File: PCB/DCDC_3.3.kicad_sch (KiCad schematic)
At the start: 21 parts, among them U1 HT75xx-1-SOT89, U10 LV2842XLVDDCR

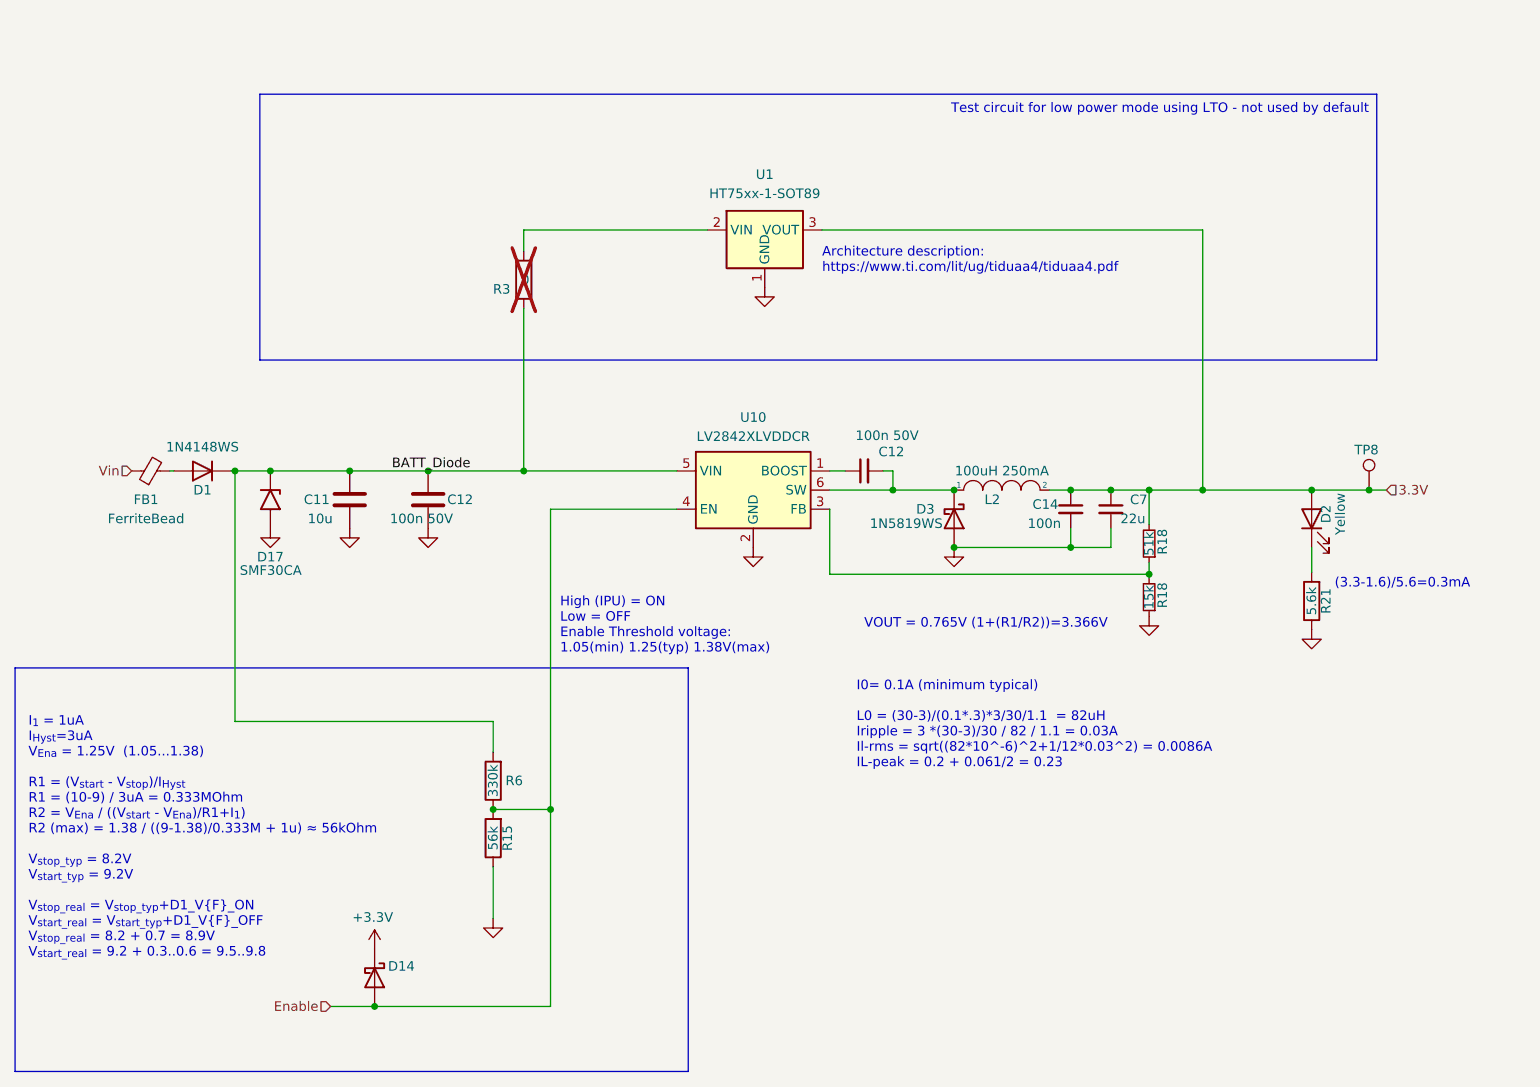
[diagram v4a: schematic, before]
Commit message: Added jumper for the DCDC enable line
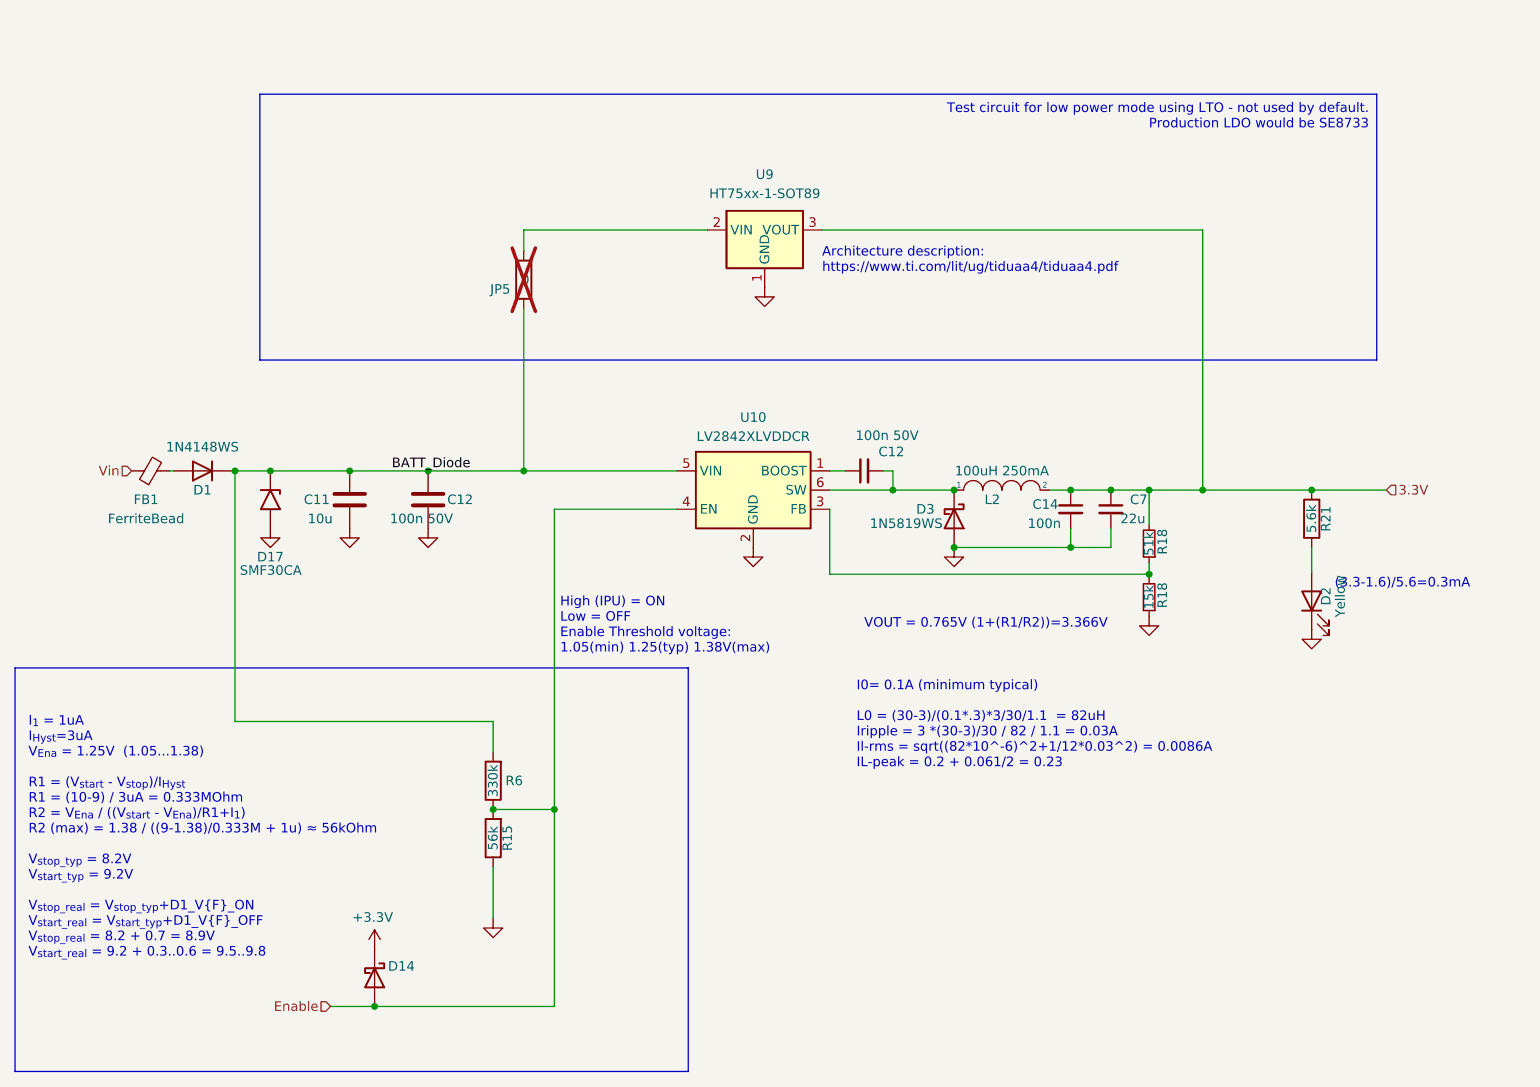
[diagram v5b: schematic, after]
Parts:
- removed TP8: WirePad, TestPoint:TestPoint_Pad_D1.0mm, symbol Connector:TestPoint
- renumbered R3 to JP5, U1 to U9
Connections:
- net 3.3V: now also R21.2; no longer D2.2 (A)
- net GND: now also D2.1 (K); no longer R21.1
- new net: D2.2 (A), R21.1
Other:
- moved on the sheet: D2, R21

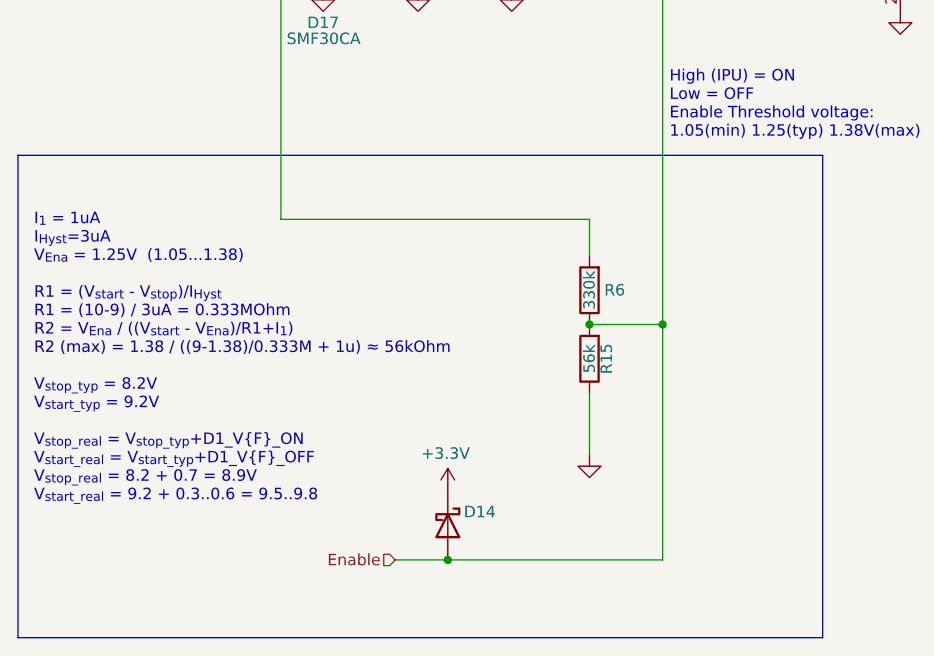
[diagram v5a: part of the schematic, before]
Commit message: Added undervoltage shutdown filter
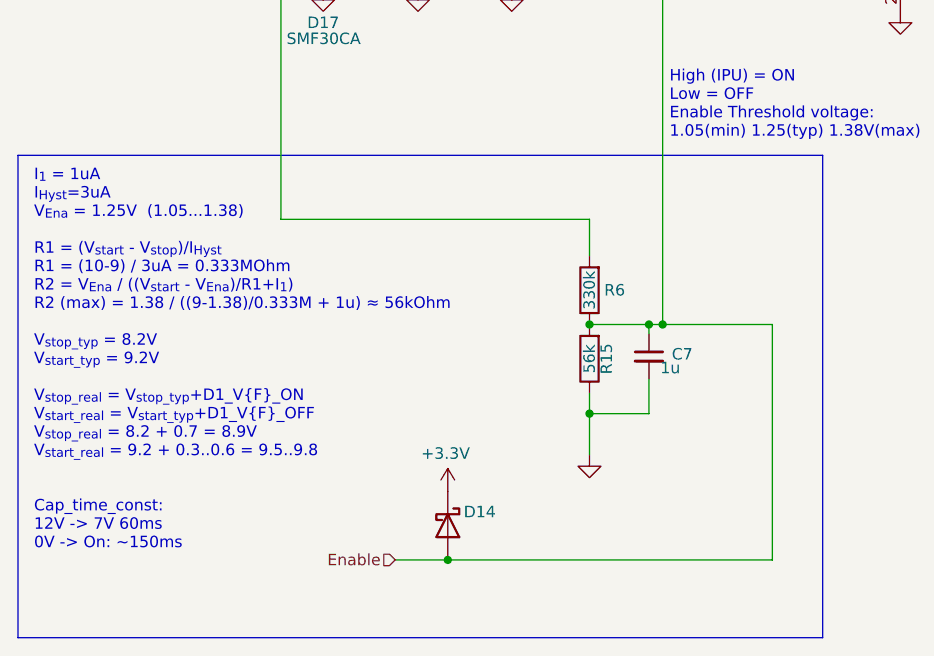
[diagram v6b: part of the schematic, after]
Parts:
- added C7: 1u, Capacitor_SMD:C_0402_1005Metric, symbol Device:C_Small
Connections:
- net Enable: now also C7.1
- net GND: now also C7.2
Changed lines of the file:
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@@
 (kicad_sch (version 20230121) (generator eeschema)
   (paper "A4")
+  (junction (at 101.6 134.874) (diameter 0) (color 0 0 0 0)
+  )
   (junction (at 105.664 80.01) (diameter 0) (color 0 0 0 0)
   )
@@
   (junction (at 178.308 82.55) (diameter 0) (color 0 0 0 0)
   )
+  (junction (at 108.204 124.968) (diameter 0) (color 0 0 0 0)
+  )
   (junction (at 82.55 80.01) (diameter 0) (color 0 0 0 0)
   )
@@
     (stroke (width 0) (type default))
   )
+  (wire (pts (xy 121.92 124.968) (xy 109.728 124.968))
+    (stroke (width 0) (type default))
+  )
   (wire (pts (xy 195.834 82.55) (xy 210.312 82.55))
     (stroke (width 0) (type default))
@@
     (stroke (width 0) (type default))
   )
+  (wire (pts (xy 108.204 124.968) (xy 109.728 124.968))
+    (stroke (width 0) (type default))
+  )
   (wire (pts (xy 188.722 92.202) (xy 188.722 93.726))
     (stroke (width 0) (type default))
@@
     (stroke (width 0) (type default))
   )
+  (wire (pts (xy 108.204 131.064) (xy 108.204 134.874))
+    (stroke (width 0) (type default))
+  )
   (wire (pts (xy 67.31 113.284) (xy 101.6 113.284))
     (stroke (width 0) (type default))
   )
-  (wire (pts (xy 101.6 132.588) (xy 101.6 139.446))
+  (wire (pts (xy 101.6 132.588) (xy 101.6 134.874))
     (stroke (width 0) (type default))
   )
@@
     (stroke (width 0) (type default))
   )
-  (wire (pts (xy 109.728 124.968) (xy 109.728 151.13))
+  (wire (pts (xy 121.92 124.968) (xy 121.92 151.13))
     (stroke (width 0) (type default))
   )
@@
     (stroke (width 0) (type default))
   )
+  (wire (pts (xy 108.204 134.874) (xy 101.6 134.874))
+    (stroke (width 0) (type default))
+  )
   (wire (pts (xy 59.182 80.01) (xy 58.674 80.01))
     (stroke (width 0) (type default))
@@
     (stroke (width 0) (type default))
   )
+  (wire (pts (xy 108.204 125.984) (xy 108.204 124.968))
+    (stroke (width 0) (type default))
+  )
   (wire (pts (xy 162.814 90.17) (xy 178.308 90.17))
     (stroke (width 0) (type default))
@@
     (stroke (width 0) (type default))
   )
-  (wire (pts (xy 85.852 151.13) (xy 109.728 151.13))
+  (wire (pts (xy 85.852 151.13) (xy 121.92 151.13))
+    (stroke (width 0) (type default))
+  )
+  (wire (pts (xy 101.6 124.968) (xy 108.204 124.968))
     (stroke (width 0) (type default))
   )
@@
     (stroke (width 0) (type default))
   )
-  (wire (pts (xy 101.6 124.968) (xy 109.728 124.968))
+  (wire (pts (xy 101.6 134.874) (xy 101.6 139.446))
     (stroke (width 0) (type default))
   )
@@
     (effects (font (size 1.27 1.27)) (justify left bottom))
   )
-  (text "I_{1} = 1uA\nI_{Hyst}=3uA\nV_{Ena} = 1.25V  (1.05...1.38)\n\nR1 = (V_{start} - V_{stop})/I_{Hyst}\nR1 = (10-9) / 3uA = 0.333MOhm\nR2 = V_{Ena} / ((V_{start} - V_{Ena})/R1+I_{1})\nR2 (max) = 1.38 / ((9-1.38)/0.333M + 1u) ≈ 56kOhm\n\nV_{stop_typ} = 8.2V\nV_{start_typ} = 9.2V\n\nV_{stop_real} = V_{stop_typ}+D1_V{F}_ON\nV_{start_real} = V_{start_typ}+D1_V{F}_OFF\nV_{stop_real} = 8.2 + 0.7 = 8.9V\nV_{start_real} = 9.2 + 0.3..0.6 = 9.5..9.8"
-    (at 39.878 144.78 0)
-    (effects (font (size 1.27 1.27)) (justify left bottom))
+  (text "I_{1} = 1uA\nI_{Hyst}=3uA\nV_{Ena} = 1.25V  (1.05...1.38)\n\nR1 = (V_{start} - V_{stop})/I_{Hyst}\nR1 = (10-9) / 3uA = 0.333MOhm\nR2 = V_{Ena} / ((V_{start} - V_{Ena})/R1+I_{1})\nR2 (max) = 1.38 / ((9-1.38)/0.333M + 1u) ≈ 56kOhm\n\nV_{stop_typ} = 8.2V\nV_{start_typ} = 9.2V\n\nV_{stop_real} = V_{stop_typ}+D1_V{F}_ON\nV_{start_real} = V_{start_typ}+D1_V{F}_OFF\nV_{stop_real} = 8.2 + 0.7 = 8.9V\nV_{start_real} = 9.2 + 0.3..0.6 = 9.5..9.8\n\n\nCap_time_const:\n12V -> 7V 60ms\n0V -> On: ~150ms"
+    (at 39.878 150.114 0)
+    (effects (font (size 1.27 1.27)) (justify left bottom) (href "https://everycircuit.com/circuit/6478510418558976"))
   )
   (text "I0= 0.1A (minimum typical)\n\nL0 = (30-3)/(0.1*.3)*3/30/1.1  = 82uH\nIripple = 3 *(30-3)/30 / 82 / 1.1 = 0.03A\nIl-rms = sqrt((82*10^-6)^2+1/12*0.03^2) = 0.0086A\nIL-peak = 0.2 + 0.061/2 = 0.23\n\n"
@@
         )
       )
+    )
+  )
+  (symbol (lib_id "Device:C_Small") (at 108.204 128.524 0) (unit 1)
+    (in_bom yes) (on_board yes) (dnp no)
+    (property "Reference" "C7" (at 110.744 128.27 0)
+      (effects (font (size 1.27 1.27)) (justify left))
+    )
+    (property "Value" "1u" (at 109.474 129.794 0)
+      (effects (font (size 1.27 1.27)) (justify left))
+    )
+    (property "Footprint" "Capacitor_SMD:C_0402_1005Metric" (at 108.204 128.524 0)
+      (effects (font (size 1.27 1.27)) hide)
+    )
+    (property "Datasheet" "https://weblib.samsungsem.com/mlcc/mlcc-ec-data-sheet.do?partNumber=CL05A105KA5NQN" (at 108.204 128.524 0)
+      (effects (font (size 1.27 1.27)) hide)
+    )
+    (property "LCSC" "C52923" (at 110.744 127.2602 0)
+      (effects (font (size 1.27 1.27)) hide)
+    )
+    (pin "1")
+    (pin "2")
+    (instances
+      (project "StepperServoCAN"
+        (path "/92dad13e-412a-43d4-9260-9087579302b1"
+          (reference "C7") (unit 1)
+        )
+        (path "/92dad13e-412a-43d4-9260-9087579302b1/82f027ad-2d00-453d-ab1c-0ba3b5cb1ef7"
+          (reference "C38") (unit 1)
+        )
+      )

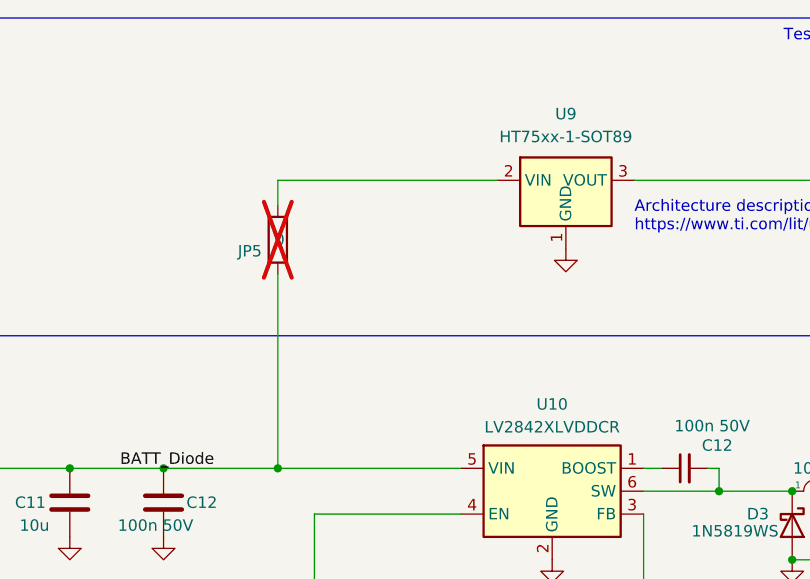
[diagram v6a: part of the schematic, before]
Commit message: Added UART/I2C aux connector
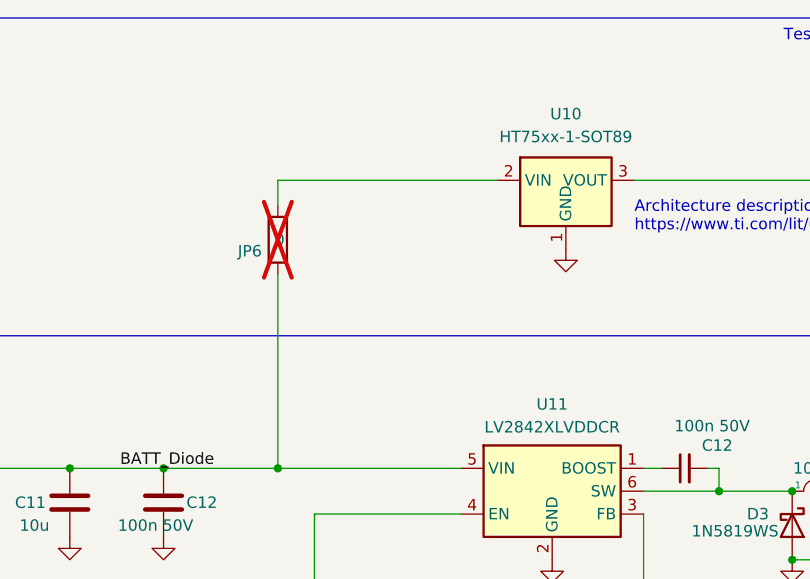
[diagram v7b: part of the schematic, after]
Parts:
- renumbered JP5 to JP6, U9 to U10, U10 to U11
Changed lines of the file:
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@@
         )
         (path "/92dad13e-412a-43d4-9260-9087579302b1/82f027ad-2d00-453d-ab1c-0ba3b5cb1ef7"
-          (reference "R47") (unit 1)
+          (reference "R49") (unit 1)
         )
       )
@@
         )
         (path "/92dad13e-412a-43d4-9260-9087579302b1/82f027ad-2d00-453d-ab1c-0ba3b5cb1ef7"
-          (reference "#PWR088") (unit 1)
+          (reference "#PWR090") (unit 1)
         )
       )
@@
         )
         (path "/92dad13e-412a-43d4-9260-9087579302b1/82f027ad-2d00-453d-ab1c-0ba3b5cb1ef7"
-          (reference "D16") (unit 1)
+          (reference "D20") (unit 1)
         )
       )
@@
         )
         (path "/92dad13e-412a-43d4-9260-9087579302b1/82f027ad-2d00-453d-ab1c-0ba3b5cb1ef7"
-          (reference "D15") (unit 1)
+          (reference "D19") (unit 1)
         )
       )
@@
         )
         (path "/92dad13e-412a-43d4-9260-9087579302b1/82f027ad-2d00-453d-ab1c-0ba3b5cb1ef7"
-          (reference "D17") (unit 1)
+          (reference "D21") (unit 1)
         )
       )
@@
         )
         (path "/92dad13e-412a-43d4-9260-9087579302b1/82f027ad-2d00-453d-ab1c-0ba3b5cb1ef7"
-          (reference "D18") (unit 1)
+          (reference "D22") (unit 1)
         )
       )
@@
         )
         (path "/92dad13e-412a-43d4-9260-9087579302b1/82f027ad-2d00-453d-ab1c-0ba3b5cb1ef7"
-          (reference "#PWR089") (unit 1)
+          (reference "#PWR091") (unit 1)
         )
       )
@@
         )
         (path "/92dad13e-412a-43d4-9260-9087579302b1/82f027ad-2d00-453d-ab1c-0ba3b5cb1ef7"
-          (reference "#PWR093") (unit 1)
+          (reference "#PWR095") (unit 1)
         )
       )
@@
   (symbol (lib_id "Regulator_Switching:LM2842X") (at 136.144 82.55 0) (unit 1)
     (in_bom yes) (on_board yes) (dnp no) (fields_autoplaced)
-    (property "Reference" "U10" (at 136.144 72.898 0)
+    (property "Reference" "U11" (at 136.144 72.898 0)
       (effects (font (size 1.27 1.27)))
     )
@@
       (project "StepperServoCAN"
         (path "/92dad13e-412a-43d4-9260-9087579302b1/82f027ad-2d00-453d-ab1c-0ba3b5cb1ef7"
-          (reference "U10") (unit 1)
+          (reference "U11") (unit 1)
         )
       )
@@
         )
         (path "/92dad13e-412a-43d4-9260-9087579302b1/82f027ad-2d00-453d-ab1c-0ba3b5cb1ef7"
-          (reference "R44") (unit 1)
+          (reference "R47") (unit 1)
         )
       )
@@
         )
         (path "/92dad13e-412a-43d4-9260-9087579302b1/82f027ad-2d00-453d-ab1c-0ba3b5cb1ef7"
-          (reference "#PWR091") (unit 1)
+          (reference "#PWR093") (unit 1)
         )
       )
@@
         )
         (path "/92dad13e-412a-43d4-9260-9087579302b1/82f027ad-2d00-453d-ab1c-0ba3b5cb1ef7"
-          (reference "#PWR090") (unit 1)
+          (reference "#PWR092") (unit 1)
         )
       )
@@
         )
         (path "/92dad13e-412a-43d4-9260-9087579302b1/82f027ad-2d00-453d-ab1c-0ba3b5cb1ef7"
-          (reference "#PWR092") (unit 1)
+          (reference "#PWR094") (unit 1)
         )
       )
@@
         )
         (path "/92dad13e-412a-43d4-9260-9087579302b1/82f027ad-2d00-453d-ab1c-0ba3b5cb1ef7"
-          (reference "#PWR094") (unit 1)
+          (reference "#PWR096") (unit 1)
         )
       )
@@
         )
         (path "/92dad13e-412a-43d4-9260-9087579302b1/82f027ad-2d00-453d-ab1c-0ba3b5cb1ef7"
-          (reference "R46") (unit 1)
+          (reference "R48") (unit 1)
         )
       )
@@
         )
         (path "/92dad13e-412a-43d4-9260-9087579302b1/82f027ad-2d00-453d-ab1c-0ba3b5cb1ef7"
-          (reference "#PWR087") (unit 1)
+          (reference "#PWR089") (unit 1)
         )
       )
@@
         )
         (path "/92dad13e-412a-43d4-9260-9087579302b1/82f027ad-2d00-453d-ab1c-0ba3b5cb1ef7"
-          (reference "D14") (unit 1)
+          (reference "D18") (unit 1)
         )
       )
@@
   (symbol (lib_id "Regulator_Linear:HT75xx-1-SOT89") (at 137.668 50.546 0) (unit 1)
     (in_bom yes) (on_board yes) (dnp no) (fields_autoplaced)
-    (property "Reference" "U9" (at 137.668 40.64 0)
+    (property "Reference" "U10" (at 137.668 40.64 0)
       (effects (font (size 1.27 1.27)))
     )
@@
       (project "StepperServoCAN"
         (path "/92dad13e-412a-43d4-9260-9087579302b1/82f027ad-2d00-453d-ab1c-0ba3b5cb1ef7"
-          (reference "U9") (unit 1)
+          (reference "U10") (unit 1)
         )
       )
@@
         )
         (path "/92dad13e-412a-43d4-9260-9087579302b1/82f027ad-2d00-453d-ab1c-0ba3b5cb1ef7"
-          (reference "#PWR095") (unit 1)
+          (reference "#PWR097") (unit 1)
         )
       )
@@
         )
         (path "/92dad13e-412a-43d4-9260-9087579302b1/82f027ad-2d00-453d-ab1c-0ba3b5cb1ef7"
-          (reference "#PWR086") (unit 1)
+          (reference "#PWR088") (unit 1)
         )
       )
@@
         )
         (path "/92dad13e-412a-43d4-9260-9087579302b1/82f027ad-2d00-453d-ab1c-0ba3b5cb1ef7"
-          (reference "R43") (unit 1)
+          (reference "R46") (unit 1)
         )
       )
@@
   (symbol (lib_id "Device:R") (at 105.664 54.61 180) (unit 1)
     (in_bom no) (on_board yes) (dnp yes)
-    (property "Reference" "JP5" (at 103.886 55.88 0)
+    (property "Reference" "JP6" (at 103.886 55.88 0)
       (effects (font (size 1.27 1.27)) (justify left))
     )
@@
       (project "StepperServoCAN"
         (path "/92dad13e-412a-43d4-9260-9087579302b1/82f027ad-2d00-453d-ab1c-0ba3b5cb1ef7"
-          (reference "JP5") (unit 1)
-        )
-      )
+          (reference "JP6") (unit 1)
+        )
+      )
